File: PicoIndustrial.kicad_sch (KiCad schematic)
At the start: 163 parts, among them IC1 LM258D, IC2 LM258D, J1 PICO, J2 WJ15EDGVC-3.81-10P, J3 WJ15EDGVC-3.81-10P, J4 WJ15EDGVC-3.81-10P, J5 WJ15EDGVC-3.81-3P, J6 USB_B_Micro, K1 HF46F_024-HS1T, K2 HF46F_024-HS1T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

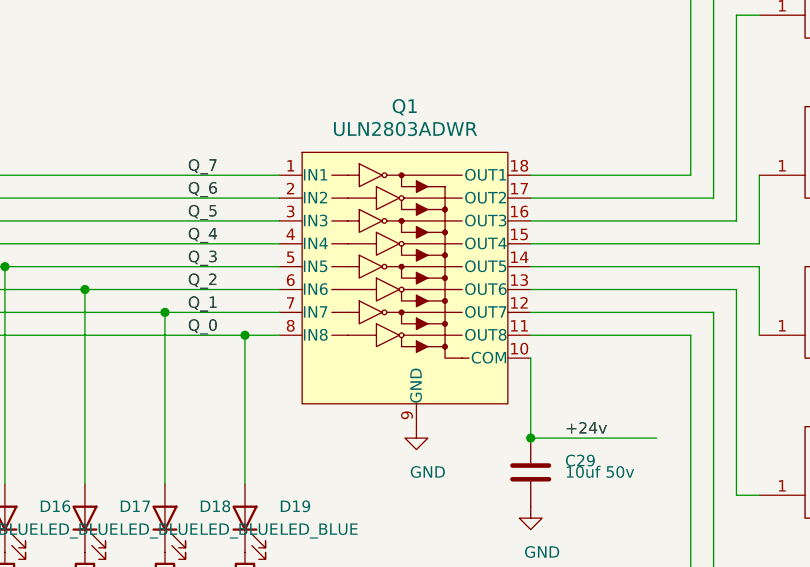
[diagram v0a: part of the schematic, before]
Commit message: Update 3d modules
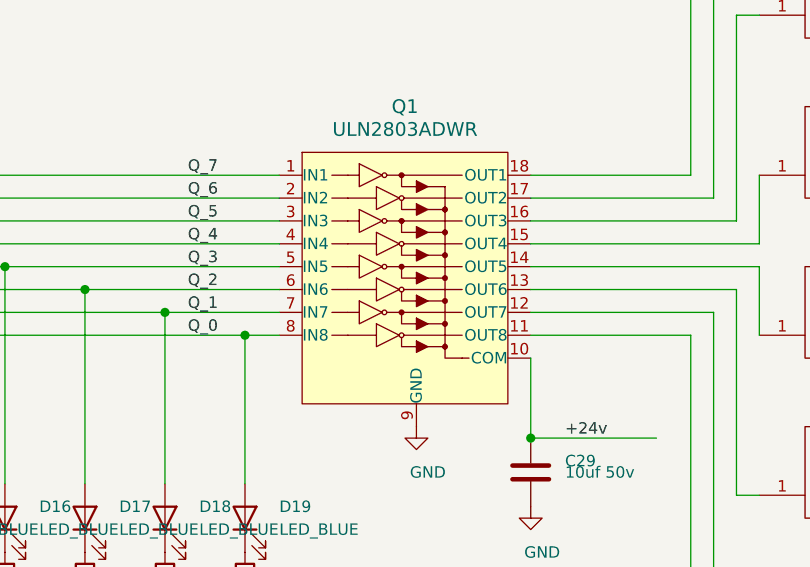
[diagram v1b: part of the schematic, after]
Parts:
- removed Q1: ULN2803ADWR, digikey-footprints:SOIC-18_W7.5mm, symbol dk_Transistors-Bipolar-BJT-Arrays:ULN2803ADWR
- added Q1: ULN2803ADWR, Package_SO:SOIC-18W_7.5x11.6mm_P1.27mm, symbol New_Library:ULN2803ADWR
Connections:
- net +24v: now also Q1.10 (COM)
- net GND: now also Q1.9 (GND)
- net Q_0: now also Q1.8 (IN8)
- net Q_1: now also Q1.7 (IN7)
- net Q_2: now also Q1.6 (IN6)
- net Q_3: now also Q1.5 (IN5)
- net Q_4: now also Q1.4 (IN4)
- net Q_5: now also Q1.3 (IN3)
- net Q_6: now also Q1.2 (IN2)
- net Q_7: now also Q1.1 (IN1)
- net at K8.1 (COIL_1): now also Q1.11 (OUT8)
- net at K7.1 (COIL_1): now also Q1.12 (OUT7)
- net at K2.1 (COIL_1): now also Q1.17 (OUT2)
- net at K1.1 (COIL_1): now also Q1.18 (OUT1)
- net at K6.1 (COIL_1): now also Q1.13 (OUT6)
- net at K5.1 (COIL_1): now also Q1.14 (OUT5)
- net at K4.1 (COIL_1): now also Q1.15 (OUT4)
- net at K3.1 (COIL_1): now also Q1.16 (OUT3)
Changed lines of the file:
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@@
   (junction (at 551.18 233.68) (diameter 1.016) (color 0 0 0 0))
   (junction (at 551.18 246.38) (diameter 1.016) (color 0 0 0 0))
-  (no_connect (at 527.05 142.24))
   (no_connect (at 544.83 210.82))
-  (no_connect (at 241.3 44.45))
-  (no_connect (at 524.51 269.24))
   (no_connect (at 544.83 215.9))
+  (no_connect (at 527.05 142.24))
   (no_connect (at 529.59 142.24))
-  (no_connect (at 529.59 269.24))
   (no_connect (at 565.15 176.53))
+  (no_connect (at 524.51 269.24))
+  (no_connect (at 241.3 44.45))
   (no_connect (at 532.13 142.24))
+  (no_connect (at 529.59 269.24))
   (wire (pts (xy 34.29 41.91) (xy 34.29 54.61))
     (stroke (width 0) (type solid) (color 0 0 0 0))
@@
     )
   )
-  (symbol (lib_id "dk_Transistors-Bipolar-BJT-Arrays:ULN2803ADWR") (at 297.18 213.36 0) (unit 1)
+  (symbol (lib_id "New_Library:ULN2803ADWR") (at 297.18 213.36 0) (unit 1)
     (in_bom yes) (on_board yes)
     (property "Reference" "Q1" (id 0) (at 288.29 185.42 0)
@@
       (effects (font (size 1.524 1.524)))
     )
-    (property "Footprint" "digikey-footprints:SOIC-18_W7.5mm" (id 2) (at 302.26 208.28 0)
+    (property "Footprint" "Package_SO:SOIC-18W_7.5x11.6mm_P1.27mm" (id 2) (at 302.26 208.28 0)
       (effects (font (size 1.524 1.524)) (justify left) hide)
     )
@@
       (effects (font (size 1.524 1.524)) (justify left) hide)
     )
-    (property "MPN" "ULN2803ADWR" (id 4) (at 297.18 213.36 0)
-      (effects (font (size 1.27 1.27)) hide)
-    )
-    (property "Manufacturer" "TI" (id 5) (at 297.18 213.36 0)
-      (effects (font (size 1.27 1.27)) hide)
-    )
   )
   (symbol (lib_id "New_Library:PICO") (at 509.27 203.2 0) (unit 1)
@@
       (reference "L1") (unit 1) (value "22uh 3A") (footprint "Inductor_SMD:L_12x12mm_H6mm")
     )
-    (path "/a59a1ed7-3097-4582-85f7-4c69d7963e67"
-      (reference "Q1") (unit 1) (value "ULN2803ADWR") (footprint "digikey-footprints:SOIC-18_W7.5mm")
+    (path "/7aee8773-94e7-4eca-bf24-a4d5ac3cbe87"
+      (reference "Q1") (unit 1) (value "ULN2803ADWR") (footprint "Package_SO:SOIC-18W_7.5x11.6mm_P1.27mm")
     )
     (path "/88ca5cac-d100-4908-b641-d47e694b1167"
